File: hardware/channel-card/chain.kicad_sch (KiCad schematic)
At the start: 35 parts, among them J501 AUDIO IN, J502 AUDIO OUT, J503 POWER IN, J504 POWER OUT, U501 LM317, U502 LM337, U503 78L05

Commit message: Check parts against LCSC stock and use basic resistor values
tools/lcsc_check.py checks docs/parts.csv against the JLCPCB/LCSC
catalogue and writes docs/lcsc-check.csv. Non-critical resistors move
to JLC basic values to cut setup fees (decision 79): bus resistors 22k,
VCA input network 100R, cutoff offset 470k, regulator dividers 200R/2k2
(15.1 V). All sheets rebuilt and verified (ERC 0/0).

Co-Authored-By: Claude Opus 5.5 <noreply@anthropic.com>
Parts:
- R501, R503: value 120 -> 200; ProjectPN SX-R-045 -> SX-R-010
- R502, R504: value 1k33 -> 2k2; ProjectPN SX-R-046 -> SX-R-049

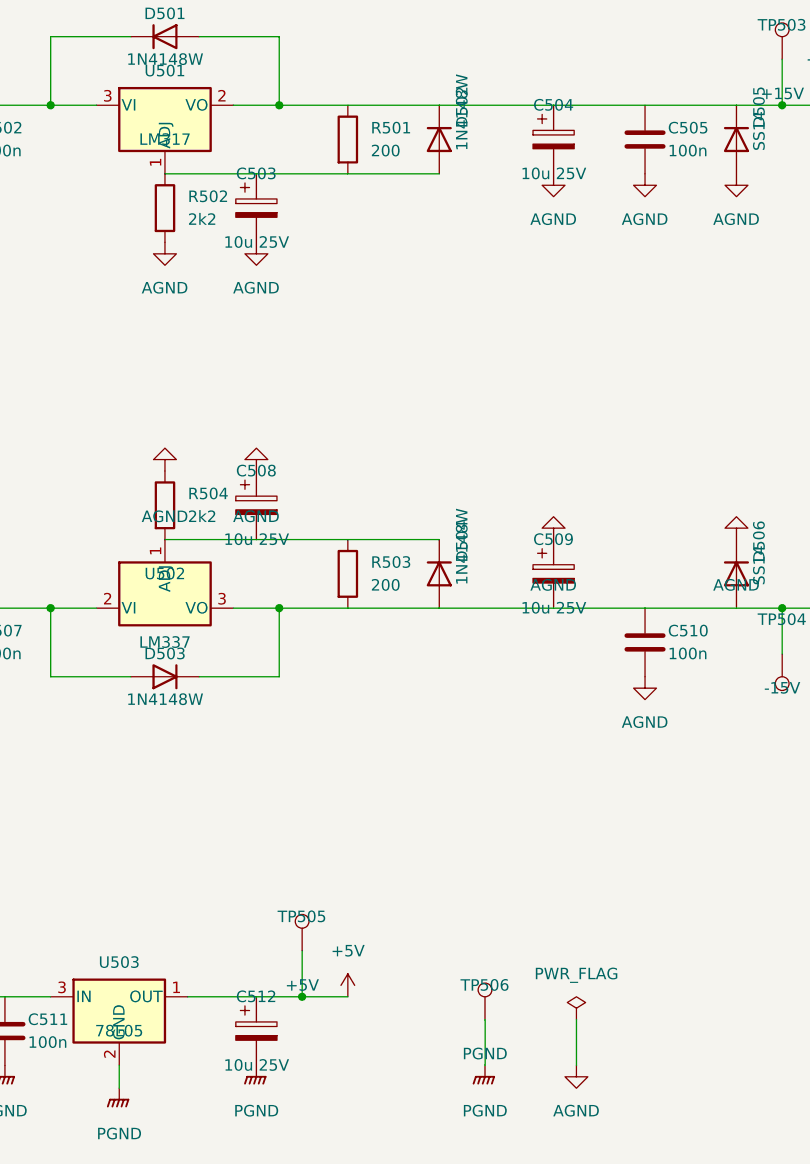
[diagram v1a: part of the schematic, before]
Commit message: Channel card: mechanical parts, decisions 110-117
- 110 LM317/LM337 in D2PAK on copper (onsemi, LCSC)
- 111 SMD electrolytics <= 5.4 mm (ROQANG, Panasonic bipolar)
- 112 trimmers and jumper headers on the underside, bottom cover for /system
- 113 low-cut caps C0G 1206
- 114 pot shaft standard T18 15 mm; 115 trim stage scaled to 100k, pots chosen
  (blocked until RoHS declarations)
- 116 RoHS strict for every part and board (process)
- 117 button LED colours (JLCPCB basic 0805), Wurth chain headers
- J181 drawn as Thonkiconn 3.5 mm (pending /system), fields and footprints set,
  five sheets rebuilt, netlists match, ERC 0/0
- STATUS: seven For /system items (CV jack, 0805 meter bezel, panel screws,
  bottom cover, underside keep-out, RoHS invariant, contract doc updates)

Co-Authored-By: Claude Opus 5.5 <noreply@anthropic.com>
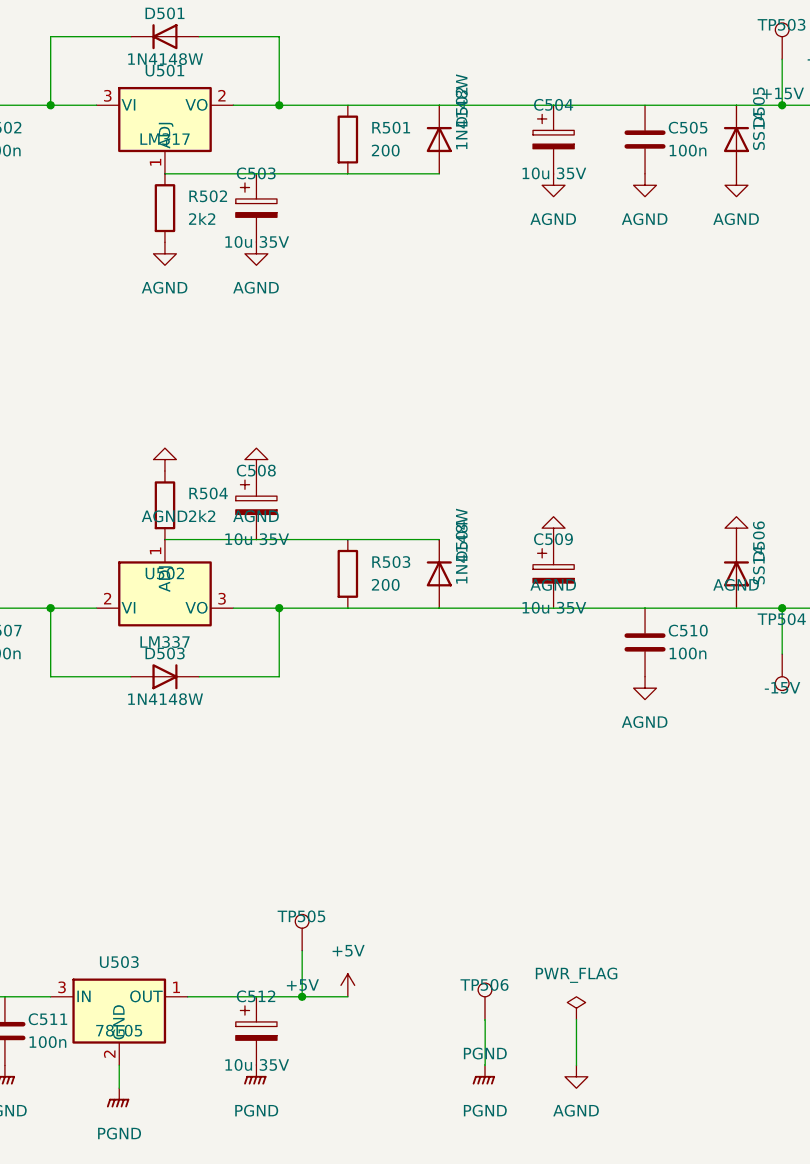
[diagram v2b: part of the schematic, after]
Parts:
- removed U501: LM317, Package_TO_SOT_THT:TO-220-3_Vertical, symbol Regulator_Linear:LM317_TO-220
- removed U502: LM337, Package_TO_SOT_THT:TO-220-3_Vertical, symbol Regulator_Linear:LM337_TO220
- added U501: LM317, Package_TO_SOT_SMD:TO-263-2, symbol Regulator_Linear:LM317_TO-263
- added U502: LM337, Package_TO_SOT_SMD:TO-263-2, symbol Regulator_Linear:LM337_TO263
- C501, C506: footprint Capacitor_THT:CP_Radial_D6.3mm_P2.50mm -> Capacitor_SMD:CP_Elec_6.3x5.4; MPN (none) -> RVT1V470M0605; Manufacturer (none) -> ROQANG; ProjectPN SX-C-011 -> SX-C-025; Supplier (none) -> LCSC; SupplierPN (none) -> C72522
- C503, C504, C508, C509, C512: value 10u 25V -> 10u 35V; footprint Capacitor_THT:CP_Radial_D5.0mm_P2.00mm -> Capacitor_SMD:CP_Elec_5x5.4; MPN (none) -> RVT1V100M0505; Manufacturer (none) -> ROQANG; ProjectPN SX-C-012 -> SX-C-024; Supplier (none) -> LCSC; SupplierPN (none) -> C72486
- J501, J502: MPN (none) -> 61203421621; Manufacturer (none) -> Wurth Elektronik; Note 34-pin shrouded keyed box header, pinout docs/CHAIN.md -> 34-pin shrouded keyed box header, pinout docs/CHAIN.md; und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; Supplier (none) -> Mouser; SupplierPN (none) -> 710-61203421621
- J503, J504: MPN (none) -> 61200821621; Manufacturer (none) -> Wurth Elektronik; Note 8-pin shrouded keyed box header: 1-2 V-, 3-6 PGND, 7-8 V+ (docs/CHAIN.md) -> 8-pin shrouded keyed box header: 1-2 V-, 3-6 PGND, 7-8 V+ (docs/CHAIN.md); underside (decision 109); Supplier (none) -> Mouser; SupplierPN (none) -> 710-61200821621
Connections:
- net +15V: now also U501.2 (VO)
- net +20V_RAW: now also U501.3 (VI)
- net -15V: now also U502.3 (VO)
- net -20V_RAW: now also U502.2 (VI)
- net at C503.1, D502.2 (A), R501.2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: now also U501.1 (ADJ)
- net at C508.2, D504.1 (K), R503.1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: now also U502.1 (ADJ)

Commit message: Channel card: fee-free TL072CDT, 78L05G-AB3-R, BZT52C6V2, UNI-ROYAL resistors (decision 137)
SX-IC-007 TL072 -> ST TL072CDT (LCSC C6961, basic), SX-IC-012 78L05 -> UTC
78L05G-AB3-R (C71136, basic; pins 1 O 2 G 3 I, not the -AB3-C-R variant),
SX-D-001 -> hongjiacheng BZT52C6V2 (C19077403, preferred), SX-R-011/036/042
-> UNI-ROYAL 0805W8F (preferred). Datasheet facts and RoHS sources in
parts.csv. Filter, level, meter and chain sheets rebuilt: netlists match,
ERC 0/0. costs.py extended: 82 -> 80 fee types. Master STATUS notes that
its TL072 symbols still need the ST fields.

Co-Authored-By: Claude Opus 5.5 <noreply@anthropic.com>
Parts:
- U503: MPN L78L05ACUTR -> 78L05G-AB3-R; Manufacturer STMicroelectronics -> UTC; Supplier (none) -> LCSC; SupplierPN (none) -> C71136

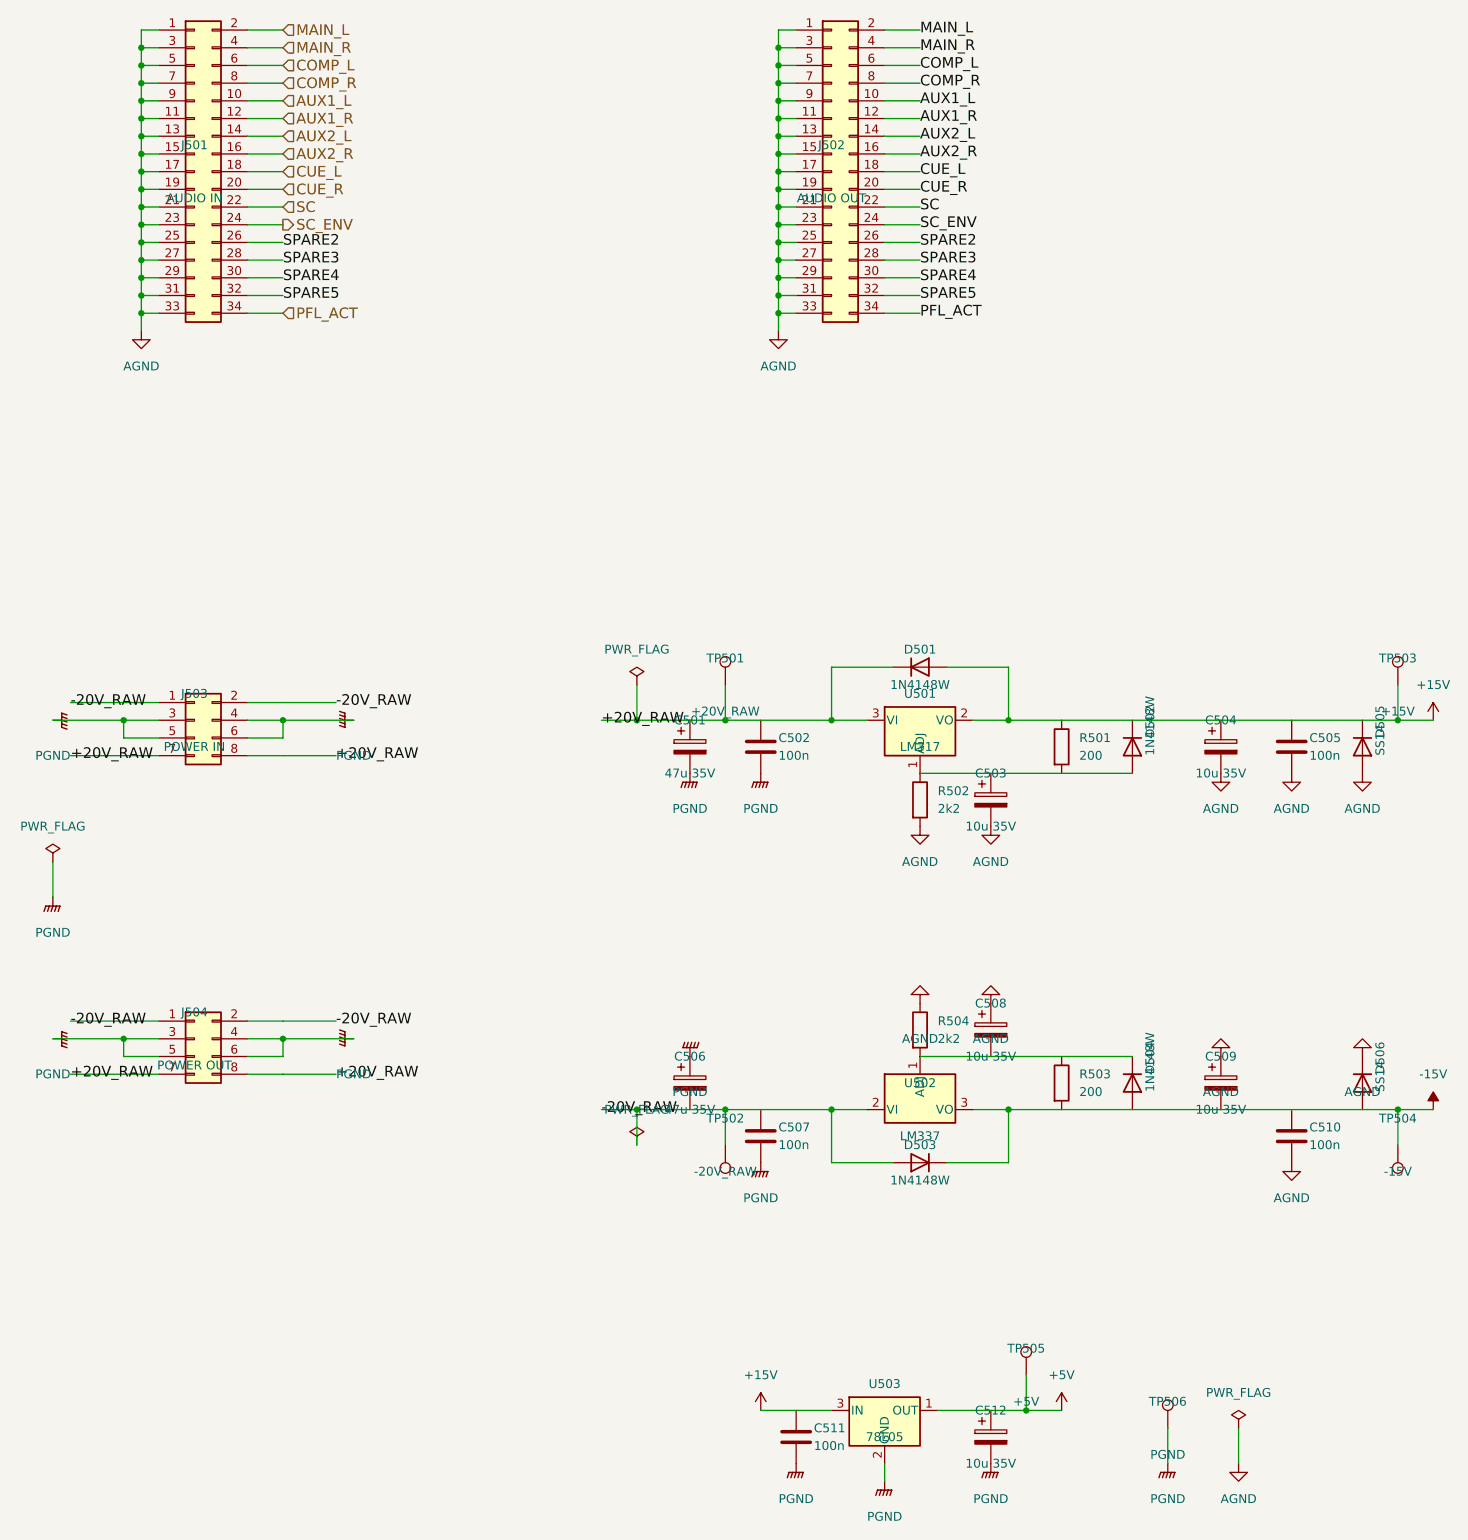
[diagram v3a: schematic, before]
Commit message: Channel card: chain sheet down to one audio and one power header on the multi-drop cables, spares unconnected; decisions 139-143 reviewed by the user (decision 175)
Co-Authored-By: Claude Opus 5.5 <noreply@anthropic.com>
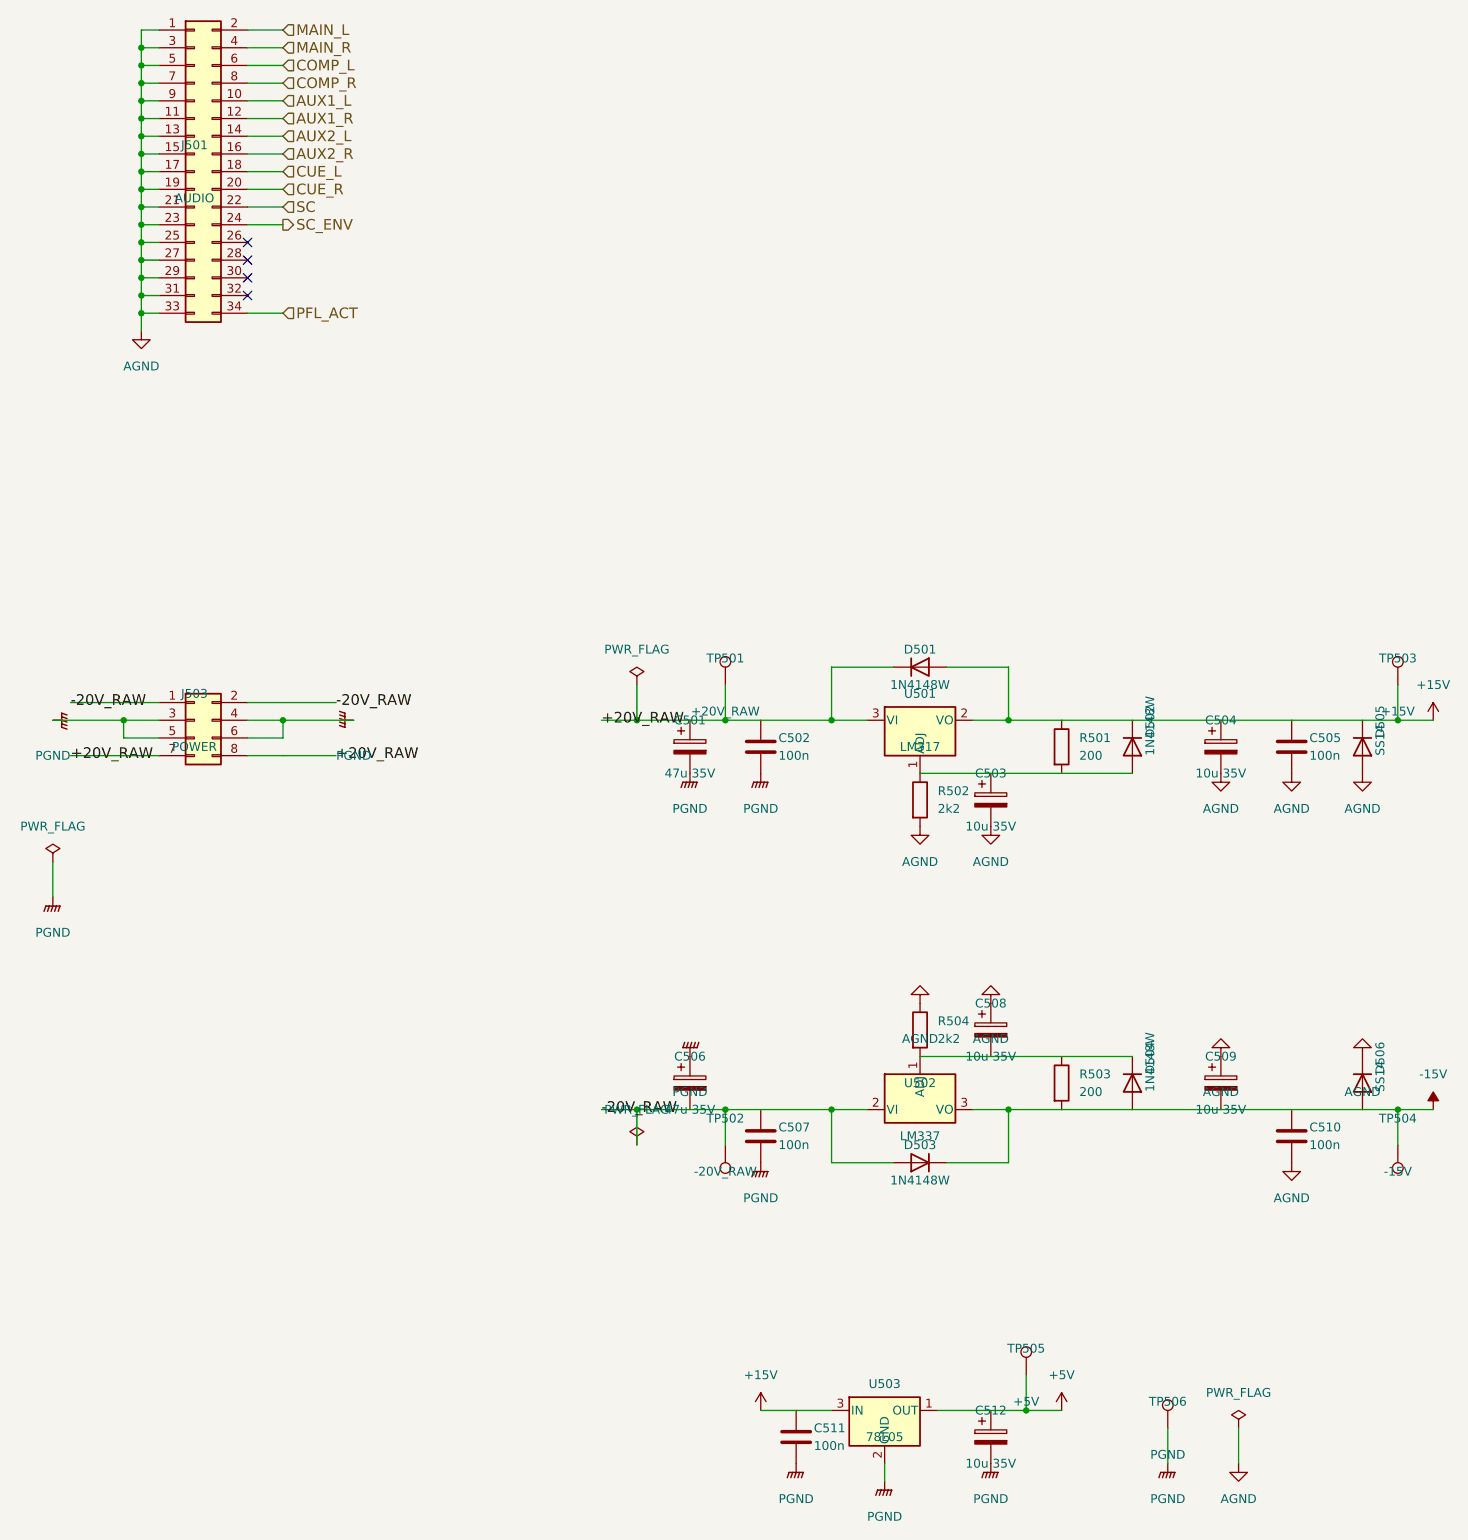
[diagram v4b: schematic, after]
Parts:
- removed J502: AUDIO OUT, Connector_IDC:IDC-Header_2x17_P2.54mm_Vertical, symbol Connector_Generic:Conn_02x17_Odd_Even
- removed J504: POWER OUT, Connector_IDC:IDC-Header_2x04_P2.54mm_Vertical, symbol Connector_Generic:Conn_02x04_Odd_Even
- J501: value AUDIO IN -> AUDIO; Note 34-pin shrouded keyed box header, pinout docs/CHAIN.md; underside (decision 109) -> 34-pin shrouded keyed box header, pinout docs/CHAIN.md; underside, pin 1 toward the front (decisions 109, 175)
- J503: value POWER IN -> POWER; Note 8-pin shrouded keyed box header: 1-2 V-, 3-6 PGND, 7-8 V+ (docs/CHAIN.md); underside (decision 109) -> 8-pin shrouded keyed box header: 1-2 V-, 3-6 PGND, 7-8 V+ (docs/CHAIN.md); underside, pin 1 toward the front (decisions 109, 175)
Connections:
- net SPARE2: no longer names the net of J501.26 (Pin_26)
- net SPARE3: no longer names the net of J501.28 (Pin_28)
- net SPARE4: no longer names the net of J501.30 (Pin_30)
- net SPARE5: no longer names the net of J501.32 (Pin_32)
- no-connect marks 0 -> 4

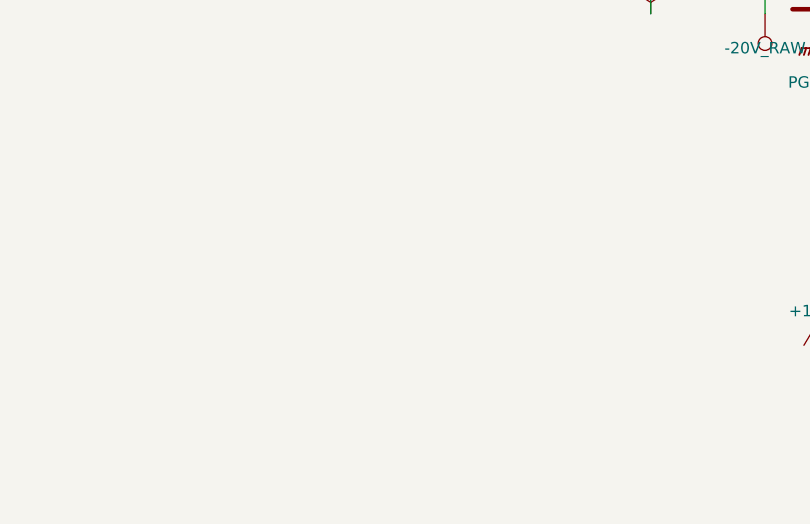
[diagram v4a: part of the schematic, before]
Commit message: Channel card: CD4052B bus assign, PFL and SC send switches at the virtual-earth bus ends, LCSC BOCHEN trimmers (decisions 183-184)
Co-Authored-By: Claude Opus 5.5 <noreply@anthropic.com>
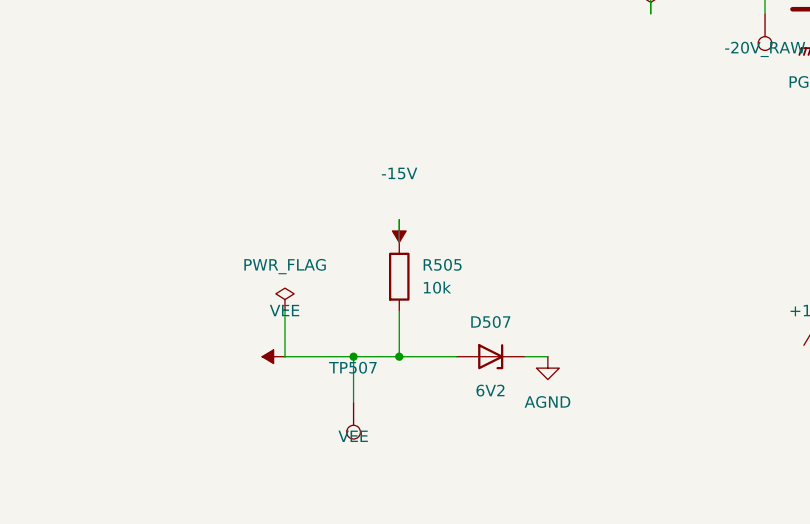
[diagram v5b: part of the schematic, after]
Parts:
- added D507: 6V2, Diode_SMD:D_SOD-123, symbol Device:D_Zener
- added R505: 10k, Resistor_SMD:R_0805_2012Metric, symbol Device:R
- added TP507: VEE, TestPoint:TestPoint_Pad_D1.5mm, symbol Connector:TestPoint
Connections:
- net -15V: now also R505.1
- net AGND: now also D507.1 (K)
- new net VEE: D507.2 (A), R505.2, TP507.1
